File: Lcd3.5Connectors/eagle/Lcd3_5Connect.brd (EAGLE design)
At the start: 11.2 x 52.5 mm, 5 parts

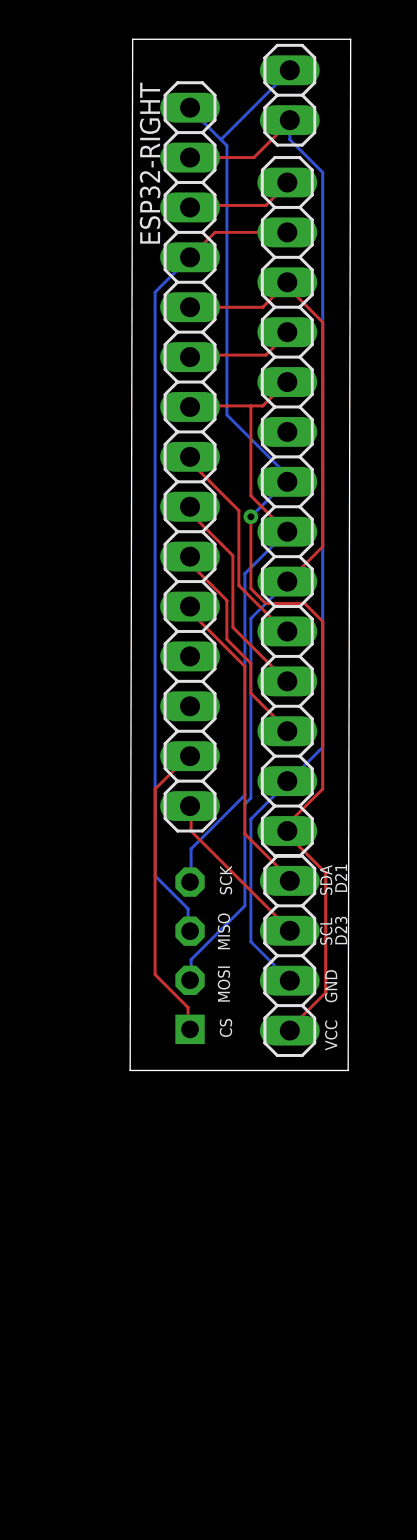
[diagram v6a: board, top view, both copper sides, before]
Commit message: Added brightness GPIO
and removed - unused - Touch IRQ pin
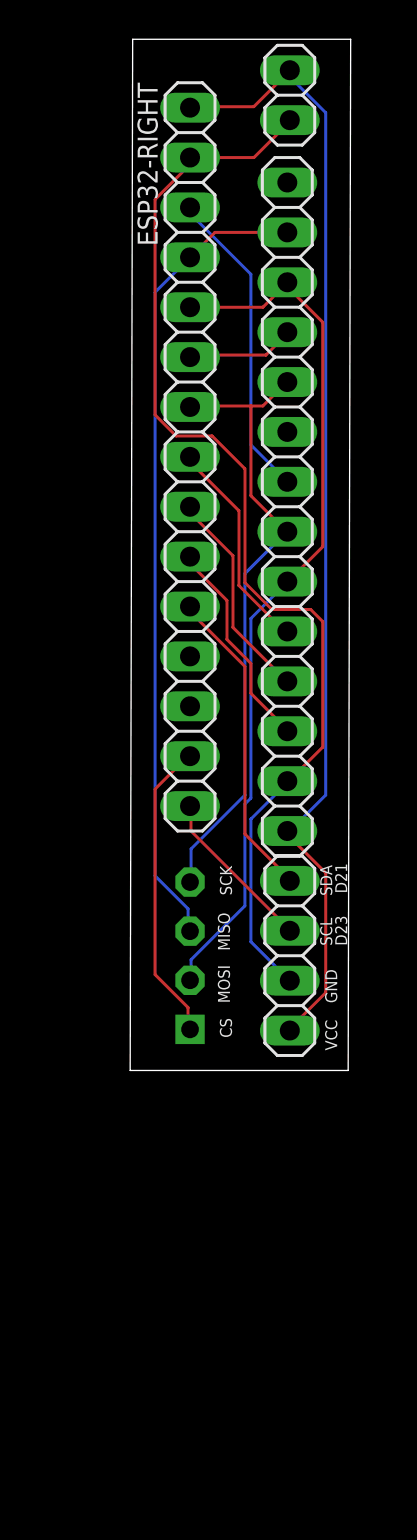
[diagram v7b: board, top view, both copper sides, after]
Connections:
- net 15: now also LCD-3.5.8; no longer LCD-3.5.14
- net 3V3: no longer LCD-3.5.8
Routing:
- net 15: track 5.54 -> 16.0 mm
- net GND: track 52.8 -> 56.7 mm
- net 3V3: track 59.8 -> 58.1 mm, vias 1 -> 0
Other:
- board text added: "LCD3.5-V4"
- board text removed: "LCD3.5-V3 T IRQ - 15 T DO - 2 T DIN - 4 T CS - 16 T CLK - 17 LCD MISO - n/c LED - VCC LCD SCK - 17 LCD MOSI - 4 LCD DC/RS - 5 RESET - 18 LCD CS - 19 GND VCC"
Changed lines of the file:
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@@
 <wire x1="10.719" y1="74.6025" x2="-0.381" y2="74.6025" width="0" layer="20"/>
 <wire x1="-0.381" y1="74.6025" x2="-0.508" y2="22.098" width="0" layer="20"/>
-<text x="10.541" y="32.4104" size="0.847596875" layer="22" distance="51" rot="MR0">LCD3.5-V3
-T IRQ - 15
-T DO - 2
-T DIN - 4
-T CS - 16
-T CLK - 17
-LCD MISO - n/c
-LED - VCC
-LCD SCK - 17
-LCD MOSI  - 4
-LCD DC/RS - 5
-RESET - 18
-LCD CS - 19
-GND
-VCC</text>
+<text x="5.969" y="73.0504" size="0.847596875" layer="22" distance="51" rot="MR0">LCD3.5-V4</text>
 <text x="4.064" y="24.765" size="0.6096" layer="21" rot="R270">CS</text>
 <text x="4.064" y="32.512" size="0.6096" layer="21" rot="R270">SCK</text>
@@
 <elements>
 <element name="ESP32-RIGHT" library="pinhead" library_urn="urn:adsk.eagle:library:325" package="1X15" package3d_urn="urn:adsk.eagle:package:22424/2" value="0" x="2.54" y="53.34" smashed="yes" rot="R270">
-<attribute name="NAME" x="0" y="72.39" size="1.016" layer="25" ratio="10" rot="R270"/>
+<attribute name="NAME" x="-0.127" y="72.39" size="1.016" layer="25" ratio="10" rot="R270"/>
 <attribute name="POPULARITY" value="4" x="-11.43" y="20.32" size="1.778" layer="27" rot="R270" display="off"/>
 </element>
@@
 <contactref element="LCD-3.5" pad="1"/>
 <contactref element="JP2" pad="1"/>
-<contactref element="LCD-3.5" pad="8"/>
 <contactref element="JP3" pad="1"/>
+<wire x1="5.7912" y1="71.1708" x2="2.5908" y2="71.1708" width="0.1524" layer="1"/>
+<wire x1="7.62" y1="72.9996" x2="5.7912" y2="71.1708" width="0.1524" layer="1"/>
+<wire x1="2.5908" y1="71.1708" x2="2.54" y2="71.12" width="0.1524" layer="1"/>
+<wire x1="7.62" y1="72.9996" x2="7.62" y2="73.025" width="0.1524" layer="1"/>
 <wire x1="7.62" y1="33.9852" x2="7.62" y2="34.29" width="0.1524" layer="1"/>
 <wire x1="9.4488" y1="32.1564" x2="7.62" y2="33.9852" width="0.1524" layer="1"/>
 <wire x1="9.4488" y1="26.0604" x2="9.4488" y2="32.1564" width="0.1524" layer="1"/>
 <wire x1="7.62" y1="24.2316" x2="9.4488" y2="26.0604" width="0.1524" layer="1"/>
+<wire x1="7.62" y1="34.29" x2="7.493" y2="34.29" width="0.1524" layer="1"/>
 <wire x1="7.62" y1="24.2316" x2="7.62" y2="24.13" width="0.1524" layer="1"/>
-<wire x1="7.4676" y1="52.4256" x2="7.4676" y2="52.1208" width="0.1524" layer="16"/>
-<wire x1="4.4196" y1="55.4736" x2="7.4676" y2="52.4256" width="0.1524" layer="16"/>
-<wire x1="4.4196" y1="69.1896" x2="4.4196" y2="55.4736" width="0.1524" layer="16"/>
-<wire x1="2.5908" y1="71.0184" x2="4.1148" y2="69.4944" width="0.1524" layer="16"/>
-<wire x1="4.1148" y1="69.4944" x2="4.4196" y2="69.1896" width="0.1524" layer="16"/>
-<wire x1="2.5908" y1="71.0184" x2="2.54" y2="71.12" width="0.1524" layer="16"/>
-<wire x1="4.1148" y1="69.4944" x2="7.62" y2="72.9996" width="0.1524" layer="16"/>
-<wire x1="7.62" y1="72.9996" x2="7.62" y2="73.025" width="0.1524" layer="16"/>
-<wire x1="7.62" y1="34.7472" x2="7.62" y2="34.29" width="0.1524" layer="1"/>
-<wire x1="9.2964" y1="36.4236" x2="7.62" y2="34.7472" width="0.1524" layer="1"/>
-<wire x1="9.2964" y1="44.958" x2="9.2964" y2="36.4236" width="0.1524" layer="1"/>
-<wire x1="8.382" y1="45.8724" x2="9.2964" y2="44.958" width="0.1524" layer="1"/>
-<wire x1="6.4008" y1="45.8724" x2="8.382" y2="45.8724" width="0.1524" layer="1"/>
-<wire x1="5.6388" y1="46.6344" x2="6.4008" y2="45.8724" width="0.1524" layer="1"/>
-<wire x1="5.6388" y1="50.292" x2="5.6388" y2="46.6344" width="0.1524" layer="1"/>
-<wire x1="7.4676" y1="52.1208" x2="5.6388" y2="50.292" width="0.1524" layer="16"/>
-<wire x1="7.62" y1="34.29" x2="7.493" y2="34.29" width="0.1524" layer="1"/>
-<wire x1="7.4676" y1="52.1208" x2="7.493" y2="52.07" width="0.1524" layer="16"/>
-<via x="5.6388" y="50.292" extent="1-16" drill="0.35"/>
+<wire x1="7.62" y1="72.6948" x2="7.62" y2="73.025" width="0.1524" layer="16"/>
+<wire x1="9.4488" y1="70.866" x2="7.62" y2="72.6948" width="0.1524" layer="16"/>
+<wire x1="9.4488" y1="36.1188" x2="9.4488" y2="70.866" width="0.1524" layer="16"/>
+<wire x1="7.62" y1="34.29" x2="9.4488" y2="36.1188" width="0.1524" layer="16"/>
+<wire x1="7.62" y1="34.29" x2="7.493" y2="34.29" width="0.1524" layer="16"/>
 </signal>
 <signal name="GND">
@@
 <wire x1="7.62" y1="26.67" x2="5.6388" y2="28.6512" width="0.1524" layer="16"/>
 <wire x1="7.4676" y1="36.7284" x2="7.493" y2="36.83" width="0.1524" layer="16"/>
-<wire x1="7.62" y1="69.4944" x2="7.62" y2="70.485" width="0.1524" layer="16"/>
-<wire x1="9.2964" y1="67.818" x2="7.62" y2="69.4944" width="0.1524" layer="16"/>
-<wire x1="9.2964" y1="38.5572" x2="9.2964" y2="67.818" width="0.1524" layer="16"/>
-<wire x1="7.62" y1="36.8808" x2="9.2964" y2="38.5572" width="0.1524" layer="16"/>
-<wire x1="7.62" y1="36.8808" x2="7.493" y2="36.83" width="0.1524" layer="16"/>
+<wire x1="2.4384" y1="68.1228" x2="2.4384" y2="68.58" width="0.1524" layer="1"/>
+<wire x1="0.762" y1="66.4464" x2="2.4384" y2="68.1228" width="0.1524" layer="1"/>
+<wire x1="0.762" y1="55.4736" x2="0.762" y2="66.4464" width="0.1524" layer="1"/>
+<wire x1="1.8288" y1="54.4068" x2="0.762" y2="55.4736" width="0.1524" layer="1"/>
+<wire x1="3.6576" y1="54.4068" x2="1.8288" y2="54.4068" width="0.1524" layer="1"/>
+<wire x1="5.334" y1="52.7304" x2="3.6576" y2="54.4068" width="0.1524" layer="1"/>
+<wire x1="5.334" y1="46.9392" x2="5.334" y2="52.7304" width="0.1524" layer="1"/>
+<wire x1="6.7056" y1="45.5676" x2="5.334" y2="46.9392" width="0.1524" layer="1"/>
+<wire x1="8.6868" y1="45.5676" x2="6.7056" y2="45.5676" width="0.1524" layer="1"/>
+<wire x1="9.2964" y1="44.958" x2="8.6868" y2="45.5676" width="0.1524" layer="1"/>
+<wire x1="9.2964" y1="38.5572" x2="9.2964" y2="44.958" width="0.1524" layer="1"/>
+<wire x1="7.62" y1="36.8808" x2="9.2964" y2="38.5572" width="0.1524" layer="1"/>
+<wire x1="2.4384" y1="68.58" x2="2.54" y2="68.58" width="0.1524" layer="1"/>
+<wire x1="7.62" y1="36.8808" x2="7.493" y2="36.83" width="0.1524" layer="1"/>
 </signal>
 <signal name="15">
 <contactref element="ESP32-RIGHT" pad="3"/>
-<contactref element="LCD-3.5" pad="14"/>
-<wire x1="6.4008" y1="66.1416" x2="2.5908" y2="66.1416" width="0.1524" layer="1"/>
-<wire x1="7.4676" y1="67.2084" x2="6.4008" y2="66.1416" width="0.1524" layer="1"/>
-<wire x1="2.5908" y1="66.1416" x2="2.54" y2="66.04" width="0.1524" layer="1"/>
-<wire x1="7.4676" y1="67.2084" x2="7.493" y2="67.31" width="0.1524" layer="1"/>
+<contactref element="LCD-3.5" pad="8"/>
+<wire x1="2.5908" y1="65.6844" x2="2.5908" y2="65.9892" width="0.1524" layer="16"/>
+<wire x1="5.6388" y1="62.6364" x2="2.5908" y2="65.6844" width="0.1524" layer="16"/>
+<wire x1="5.6388" y1="53.9496" x2="5.6388" y2="62.6364" width="0.1524" layer="16"/>
+<wire x1="7.4676" y1="52.1208" x2="5.6388" y2="53.9496" width="0.1524" layer="16"/>
+<wire x1="2.5908" y1="65.9892" x2="2.54" y2="66.04" width="0.1524" layer="16"/>
+<wire x1="7.4676" y1="52.1208" x2="7.493" y2="52.07" width="0.1524" layer="16"/>
 </signal>
 <signal name="2">
@@
 </drawing>
 <compatibility>
-<note version="6.3" minversion="6.2.2" severity="warning">
-Since Version 6.2.2 text objects can contain more than one line,
-which will not be processed correctly with this version.
-</note>
 <note version="8.2" severity="warning">
 Since Version 8.2, EAGLE supports online libraries. The ids

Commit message: Minor dimension tweak
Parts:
- moved LCD-3.5 21.9 mm to (8.26, 28.9)
- moved ESP32-RIGHT 21.9 mm to (3.17, 31.4)
- moved JP1 21.9 mm to (3.17, 6.03)
- moved JP2 21.9 mm to (8.26, 6.03)
- moved JP3 21.9 mm to (8.26, 49.8)
